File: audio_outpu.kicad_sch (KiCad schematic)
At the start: 21 parts, among them J10 NCJ6FA-H-0, J9 NCJ6FA-H-0, U7 THAT1646, U8 THAT1646

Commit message: output design update
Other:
- moved on the sheet: D10, D11, D12, D13, D6, D7, D8, D9, J10A, J10B, J9A, J9B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

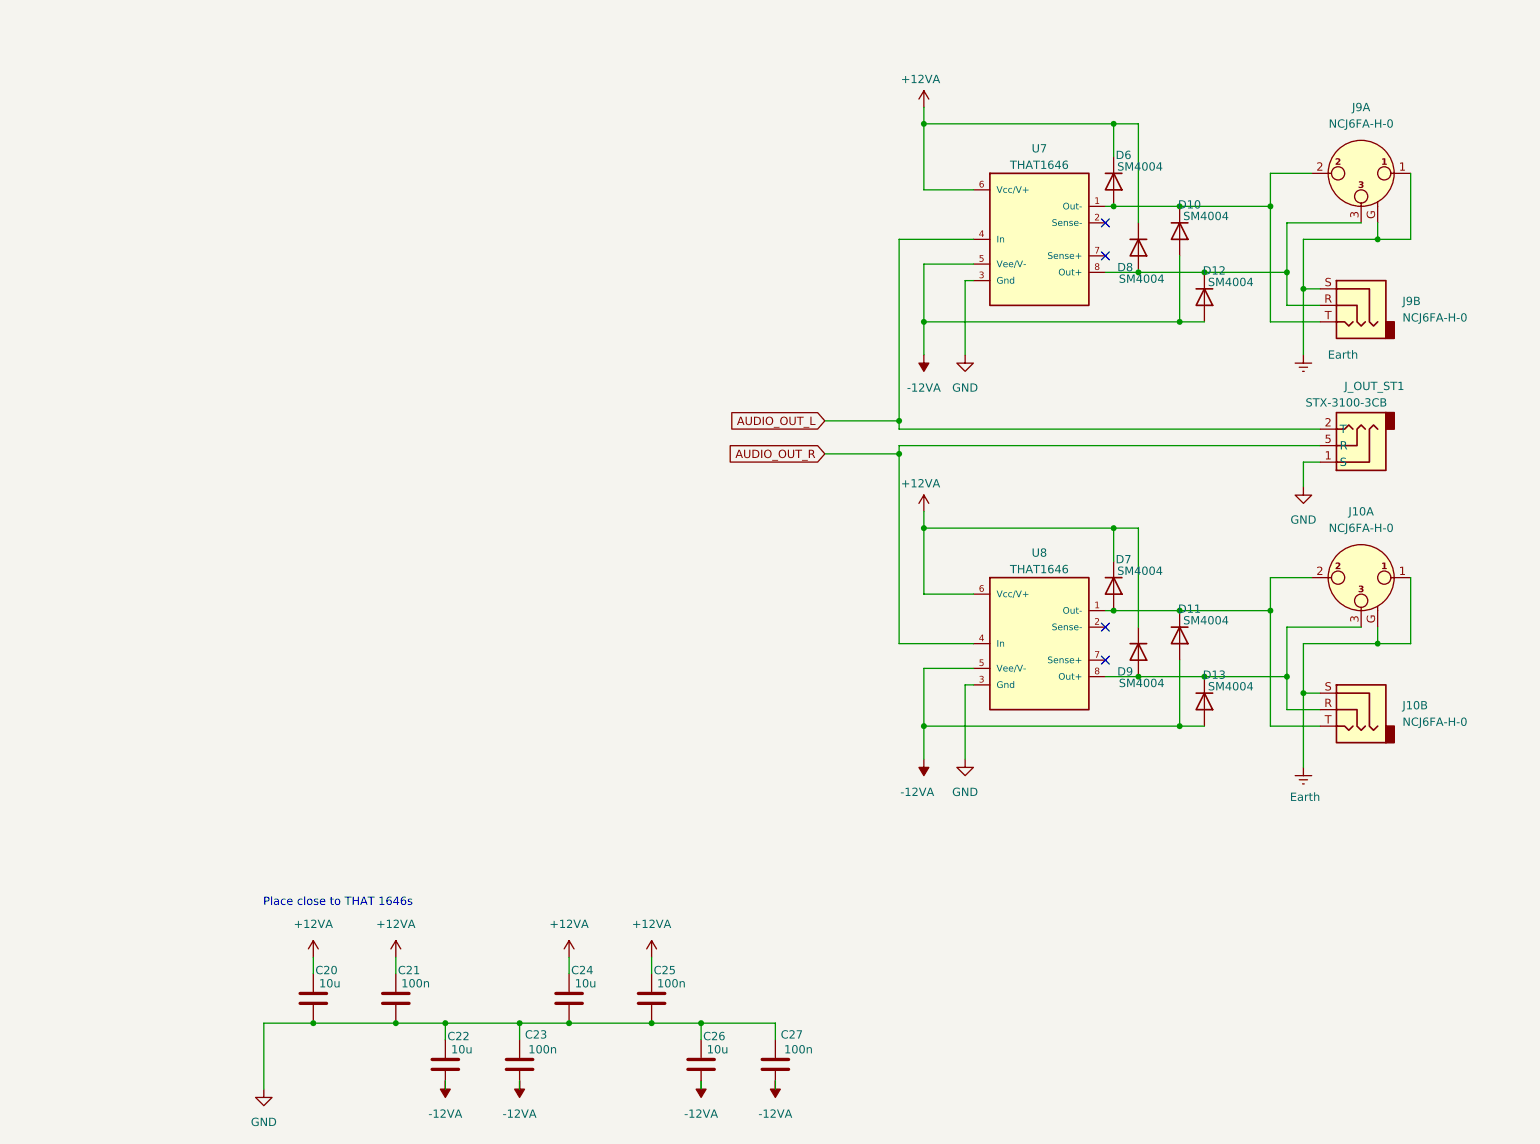
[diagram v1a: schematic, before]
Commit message: Cleanup and review of input pt 1
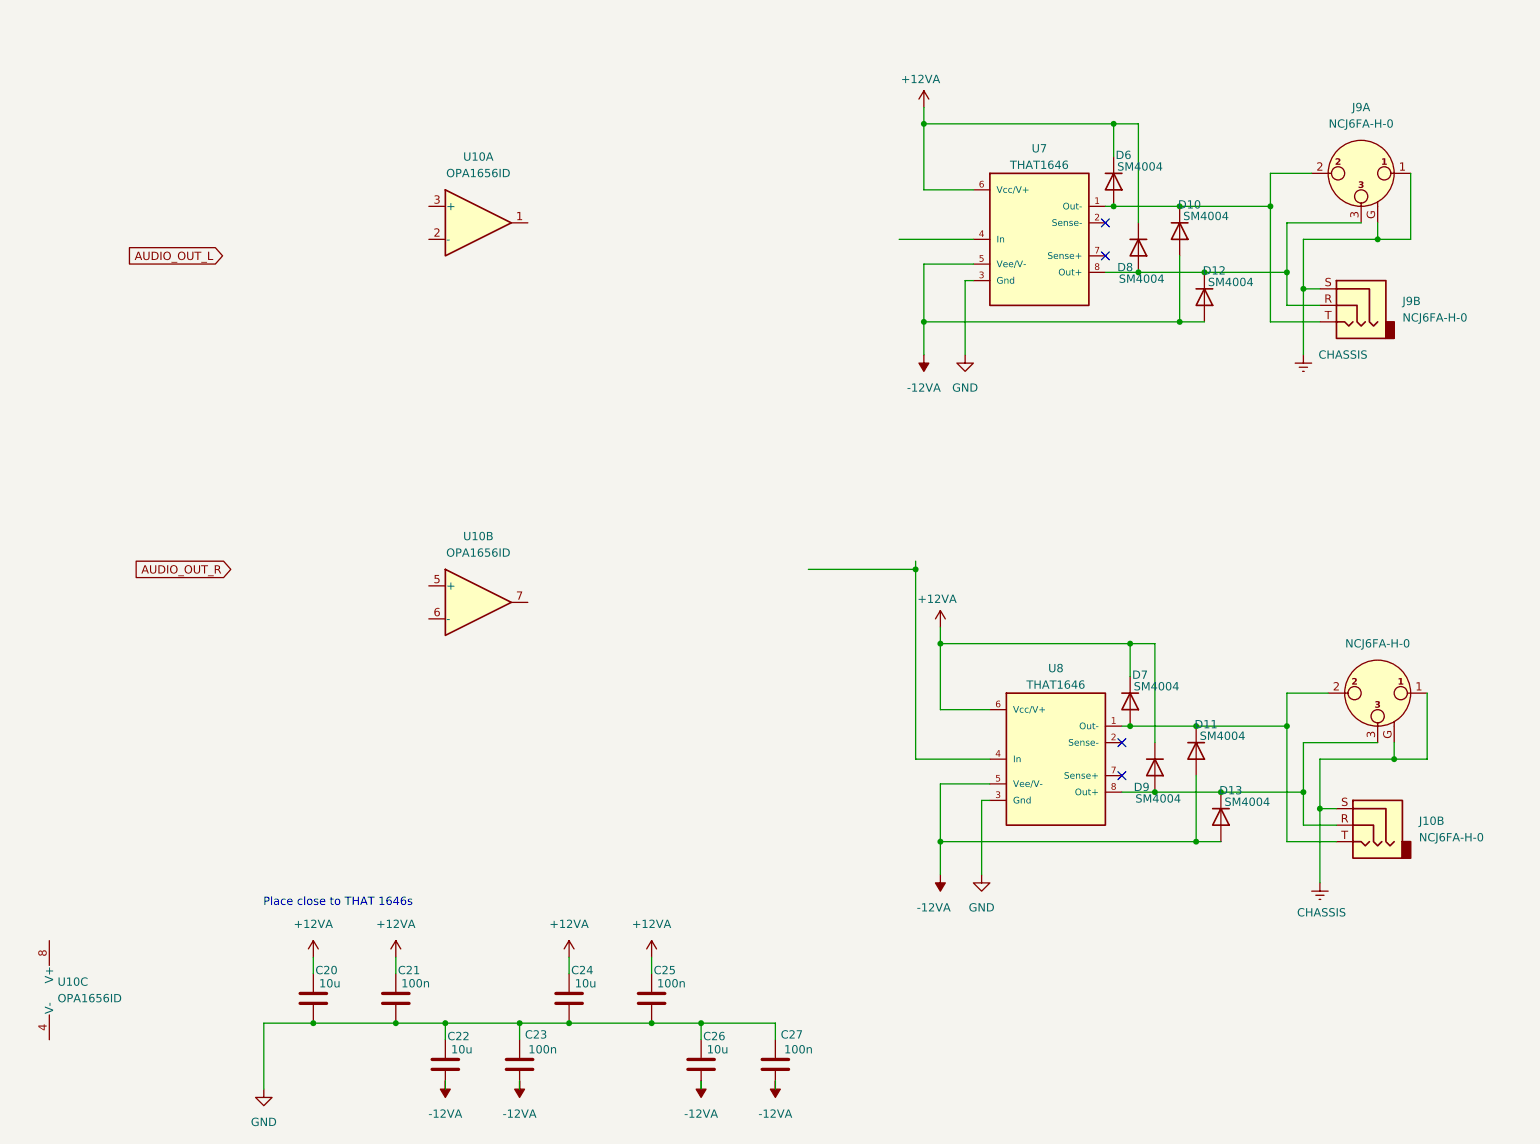
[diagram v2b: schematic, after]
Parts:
- removed J_OUT_ST1: STX-3100-3CB, Connector_Audio:Jack_3.5mm_Kycon_STX-3100-3CB, symbol Connector_Audio:AudioJack3
- added U10: OPA1656ID, Package_SO:SOIC-8_3.9x4.9mm_P1.27mm, symbol Amplifier_Operational:OPA1656ID
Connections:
- net AUDIO_OUT_L: no longer U7.4 (In)
- net AUDIO_OUT_R: no longer U8.4 (In)
- net Earth renamed CHASSIS
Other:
- moved on the sheet: D11, D13, D7, D9, J10B, U8

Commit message: fix some footprints
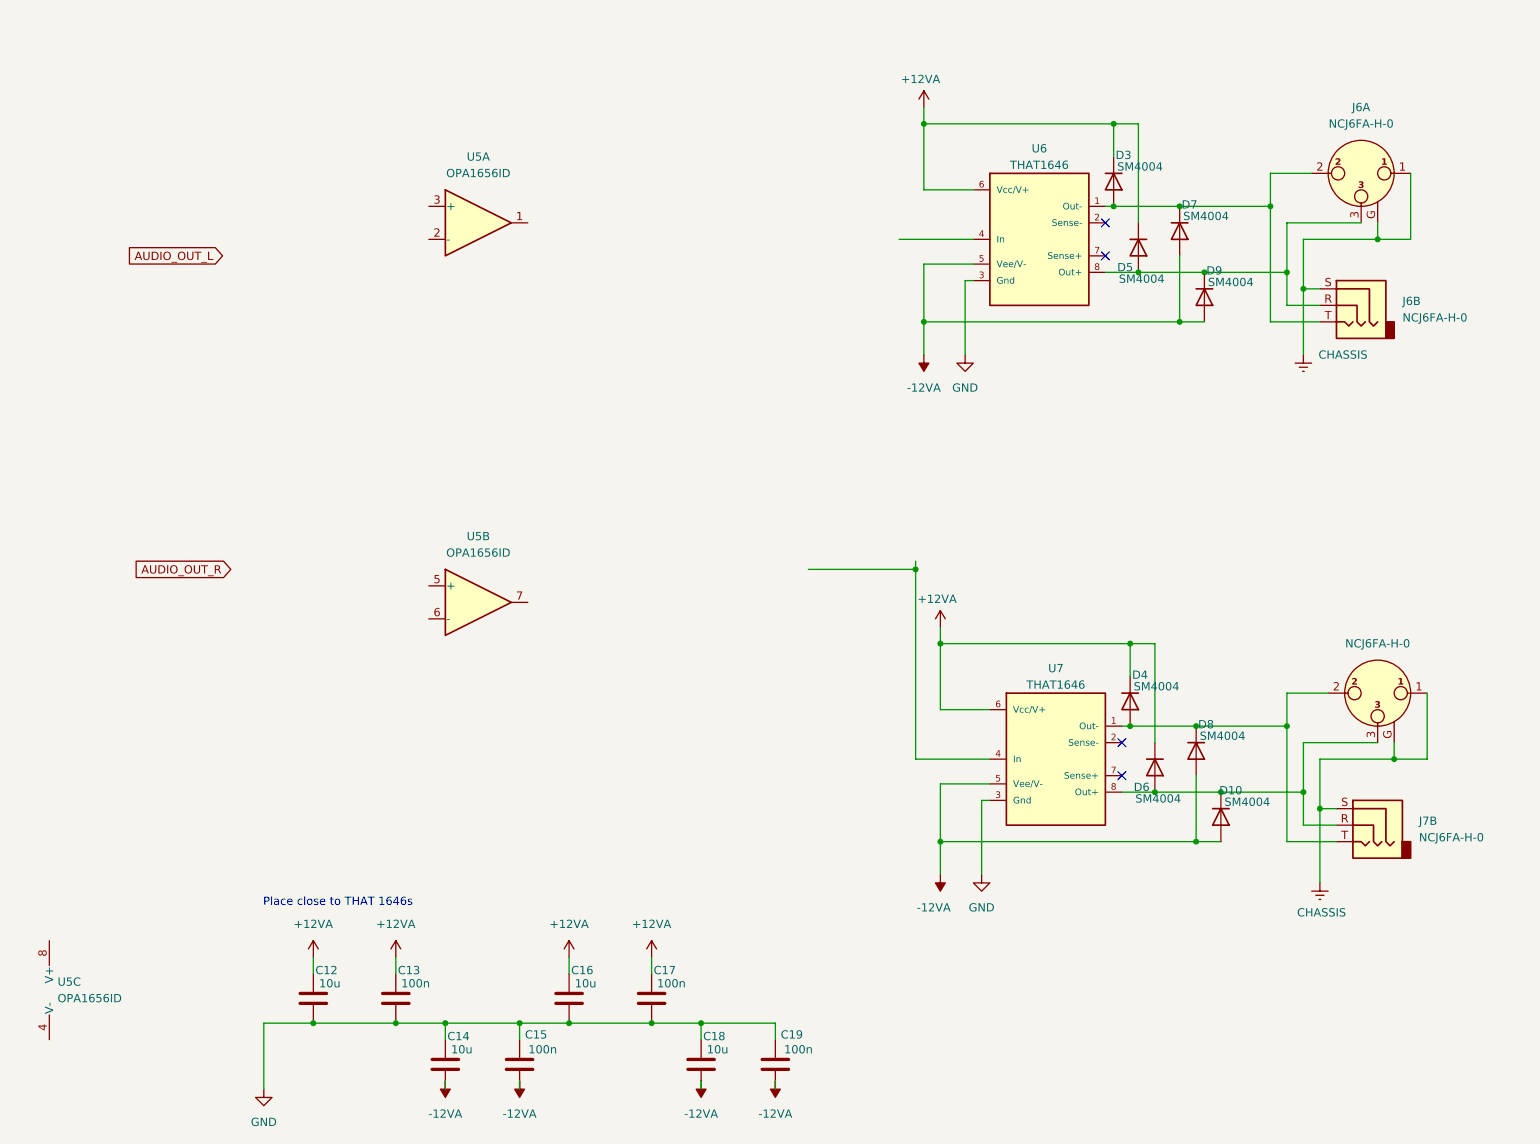
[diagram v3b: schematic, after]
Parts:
- renumbered C20 to C12, C21 to C13, C22 to C14, C23 to C15, C24 to C16, C25 to C17, C26 to C18, C27 to C19, D13 to D10, D6 to D3, D7 to D4, D8 to D5, D9 to D6, D10 to D7, D11 to D8, D12 to D9, J9 to J6, J10 to J7, U10 to U5, U7 to U6, U8 to U7

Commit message: introduce daughter board
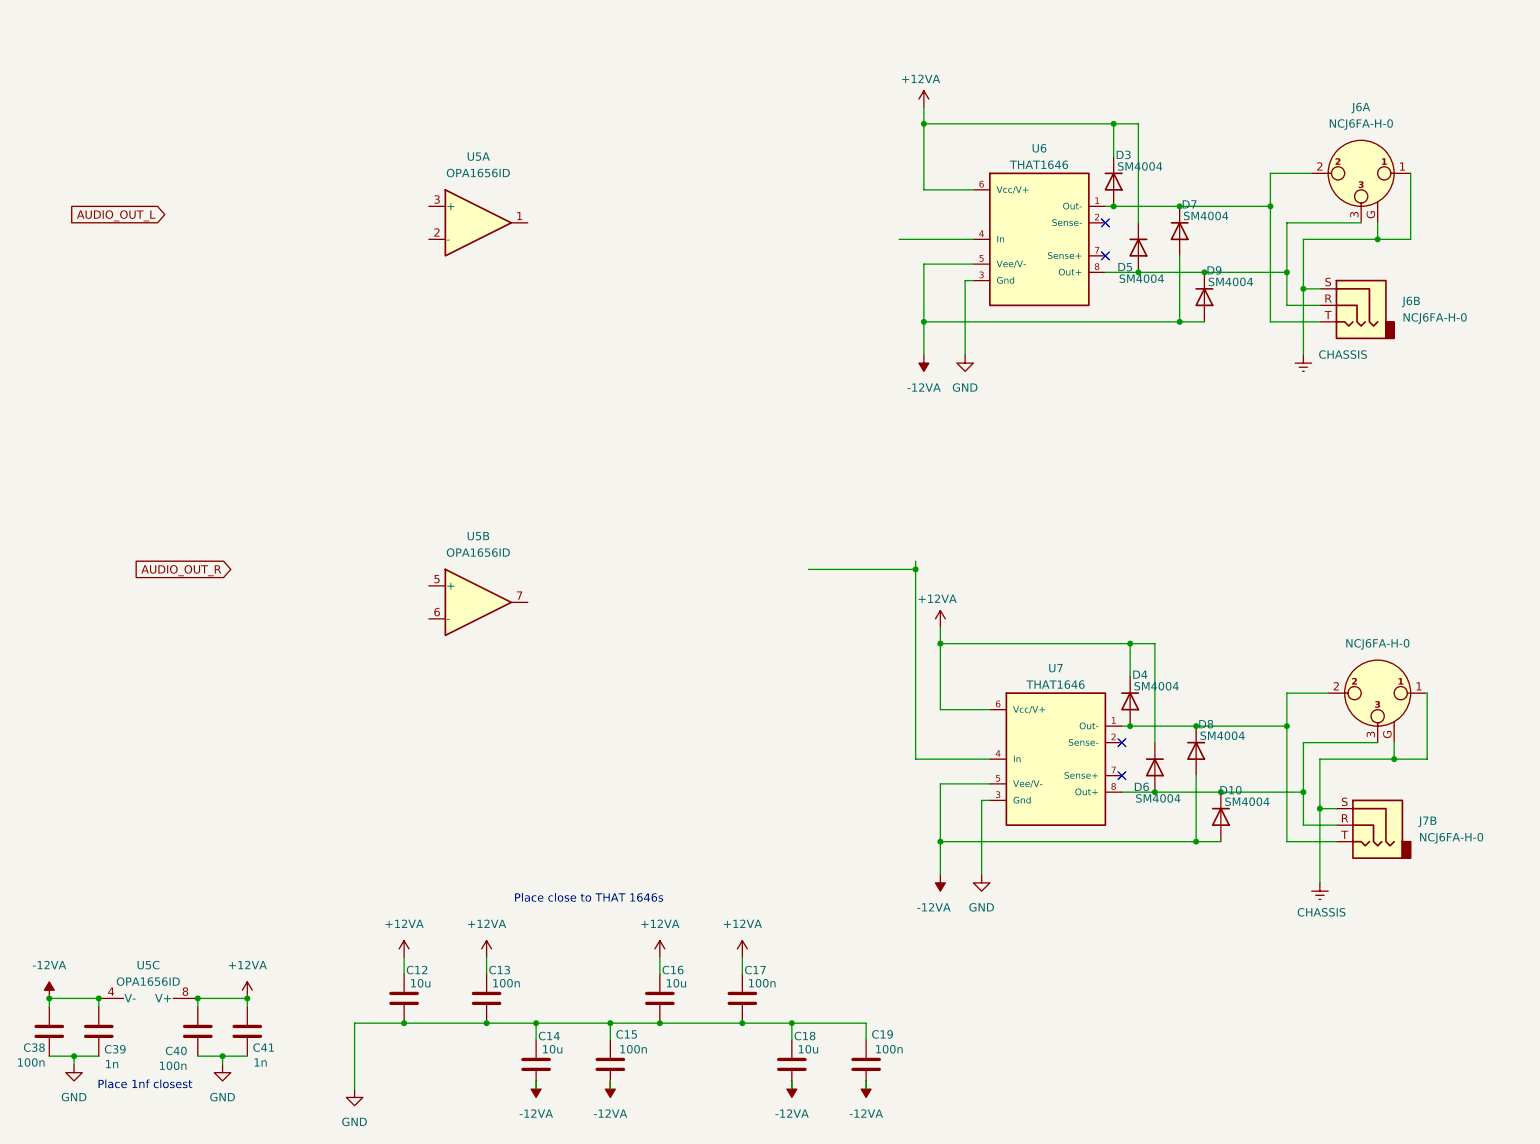
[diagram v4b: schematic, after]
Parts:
- added C38, C40: 100n, Capacitor_SMD:C_0805_2012Metric, symbol Device:C
- added C39, C41: 1n, Capacitor_SMD:C_0805_2012Metric, symbol Device:C
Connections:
- net +12VA: now also U5.8 (V+), C40.1, C41.1
- net -12VA: now also U5.4 (V-), C38.1, C39.1
- net GND: now also C38.2, C39.2, C40.2, C41.2
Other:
- note added: "Place 1nf closest"
- moved on the sheet: C12, C13, C14, C15, C16, C17, C18, C19

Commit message: starting on output
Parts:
- removed C12, C14, C16, C18: 10u, Capacitor_SMD:C_0805_2012Metric, symbol Device:C
- removed C13, C15, C17, C19, C38, C40: 100n, Capacitor_SMD:C_0805_2012Metric, symbol Device:C
- removed C39, C41: 1n, Capacitor_SMD:C_0805_2012Metric, symbol Device:C
- removed J7: NCJ6FA-H-0, Connector_Audio:Jack_XLR-6.35mm_Neutrik_NCJ6FA-H-0_Horizontal, symbol Connector_Audio:NCJ6FA-H-0
- removed unit 3 of U5
- added C42, C43: C, symbol Device:C
- added C44, C46, C49, C51, C53, C55: 100n, Capacitor_SMD:C_0805_2012Metric, symbol Device:C
- added C45, C47: 1n, Capacitor_SMD:C_0805_2012Metric, symbol Device:C
- added C48, C50, C52, C54: 10u, Capacitor_SMD:C_0805_2012Metric, symbol Device:C
- added J2: NCJ6FA-H-0, Connector_Audio:Jack_XLR-6.35mm_Neutrik_NCJ6FA-H-0_Horizontal, symbol Connector_Audio:NCJ6FA-H-0
- added R35, R36, R37, R38: R, symbol Device:R
- added RV2, RV3: R_Potentiometer_Trim, symbol Device:R_Potentiometer_Trim
- D10, D3, D4, D5, D6, D7, D8, D9: footprint Diode_SMD:D_SMA -> Diode_SMD:D_MELF
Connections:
- net +12VA: now also D8.1 (K), D9.1 (K), U5.8 (V+), C46.1, C47.1, C48.1, C49.1, C52.1, C53.1; no longer D5.1 (K), D6.1 (K)
- net -12VA: now also U5.4 (V-), C44.1, C45.1, C50.2, C51.2, C54.2, C55.2; no longer D10.2 (A), D7.2 (A), D8.2 (A), D9.2 (A)
- net AUDIO_OUT_L: now also R35.2
- net CHASSIS: now also J2.1, J2.G, J2.S
- net GND: now also D10.2 (A), D5.2 (A), D6.2 (A), D7.2 (A), U5.3 (+), U5.6 (-), C44.2, C45.2, C46.2, C47.2, C48.2, C49.2, C50.1, C51.1, C52.2, C53.2, C54.1, C55.1
- net at D4.2 (A), U7.1 (Out-): now also D6.1 (K), U7.2 (Sense-), J2.2, J2.T; no longer D8.1 (K)
- net at D10.1 (K), U7.8 (Out+): now also D8.2 (A), U7.7 (Sense+), J2.3, J2.R; no longer D6.2 (A)
- net at J6.3, J6.R, U6.8 (Out+): now also D5.1 (K), D9.2 (A), U6.7 (Sense+); no longer D5.2 (A), D9.1 (K)
- net OUT_WIPER_R: now reaches U7.4 (In)
- net OUT_OPA_L: now reaches U5.1
- net OUT_OPA_L: now also C42.2, RV2.1, RV2.2
- net at U5.2 (-): now also C42.1, R35.1, R36.2
- net at D3.2 (A), D7.1 (K), J6.2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: now also U6.2 (Sense-)
- net OUT_WIPER_L: now reaches U6.4 (In)
- net at U5.5 (+): now also C43.1, R37.1, R38.2
- net OUT_OPA_R: now reaches U5.7
- net OUT_OPA_R: now also C43.2, RV3.1, RV3.2
- new net: R38.1, RV3.3
- new net: R36.1, RV2.3
- no-connect marks 4 -> 0
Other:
- note added: "sense"
- moved on the sheet: D9, J6A, J6B, U5A, U5B, U6
